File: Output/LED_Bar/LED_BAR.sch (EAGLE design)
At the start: 19 parts

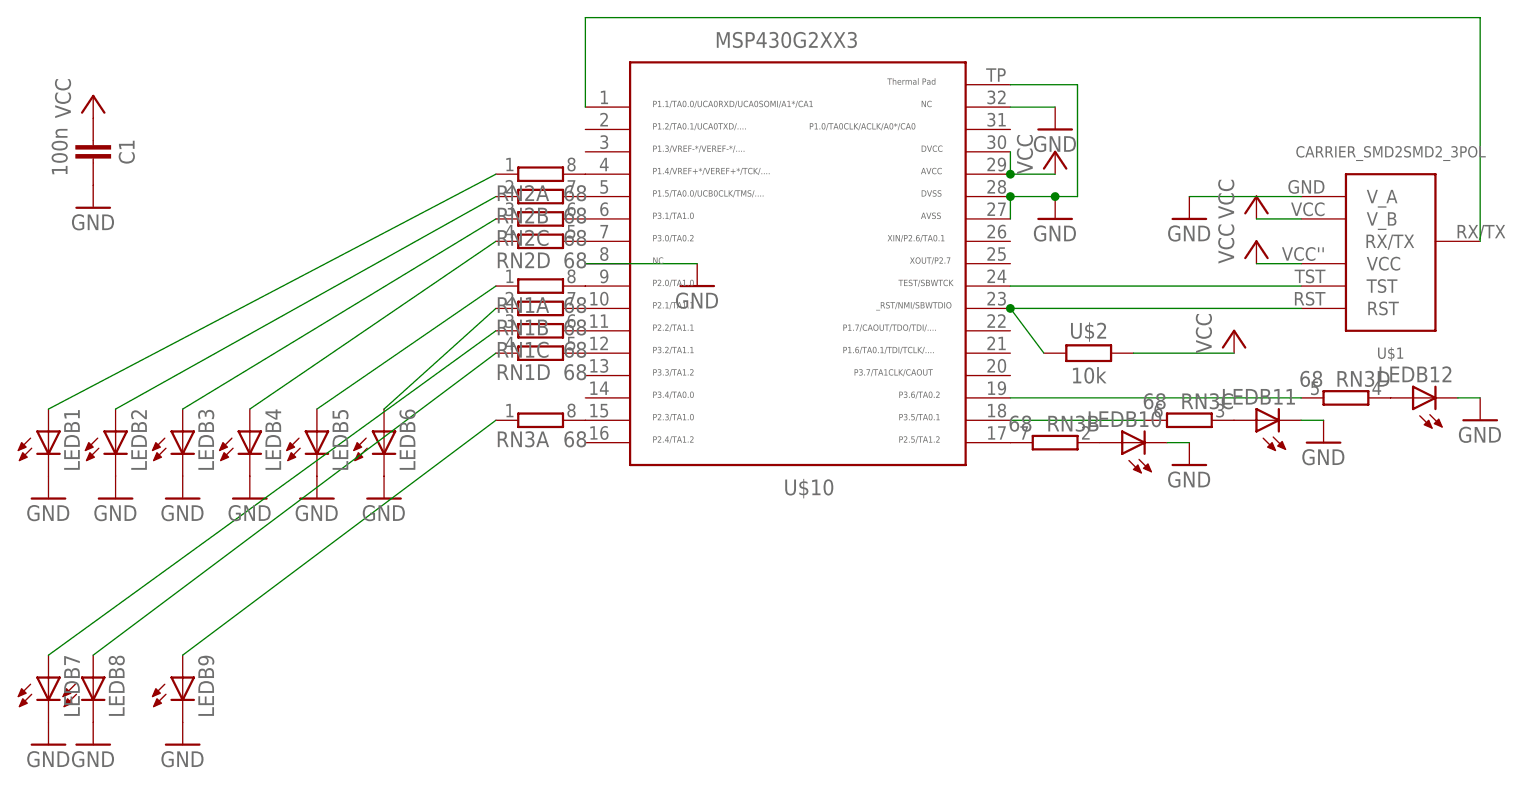
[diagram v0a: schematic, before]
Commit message: Update Pinheader
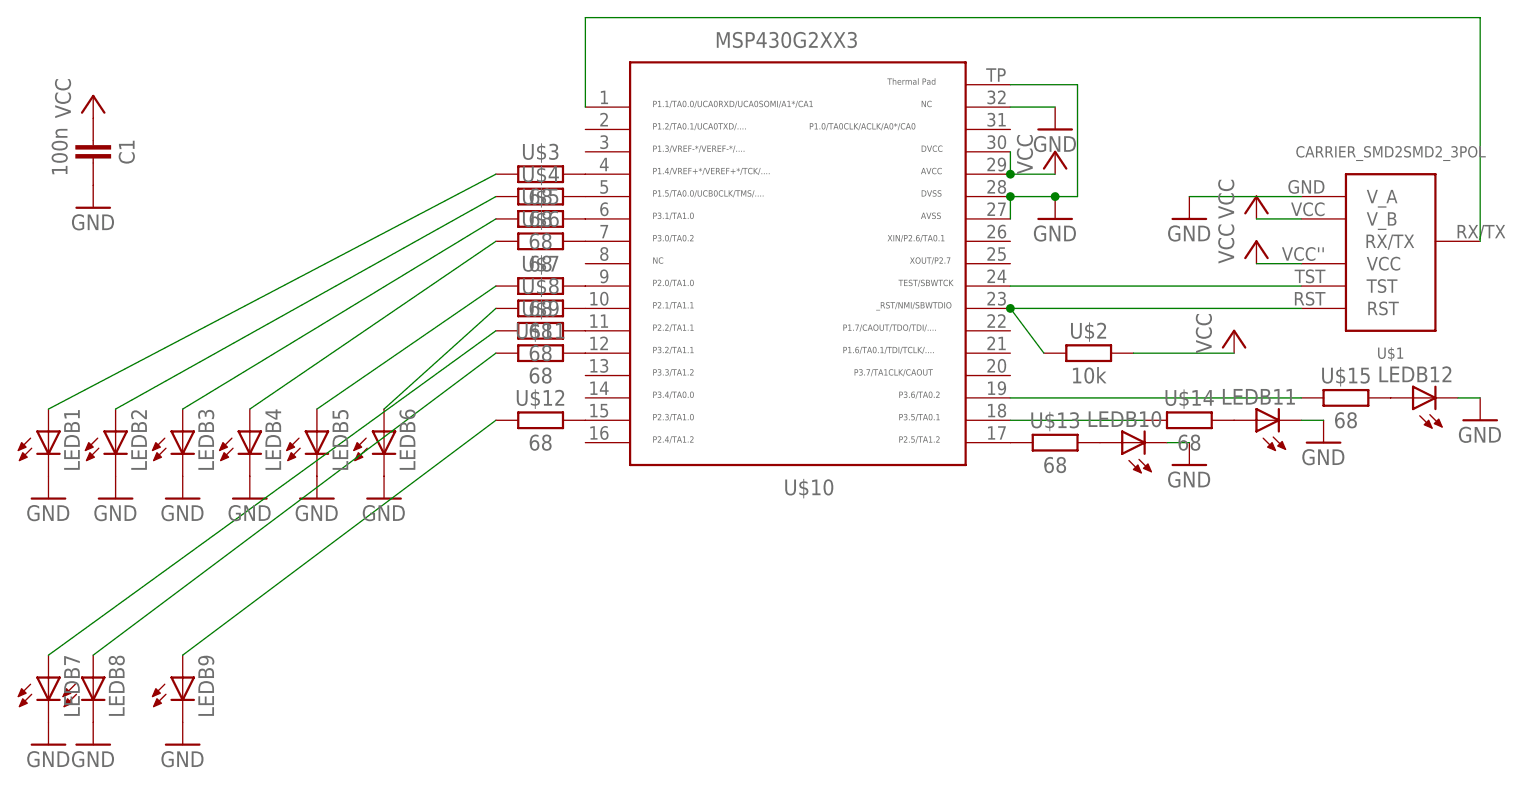
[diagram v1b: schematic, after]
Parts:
- removed RN1, RN2, RN3: 68, resistor-dil:4R-N0603-ARC
- added U$11, U$12, U$13, U$14, U$15, U$3, U$4, U$5, U$6, U$7, U$8, U$9: 68, thar:RESISTOR0603
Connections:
- net GND: no longer U$10.8
- net N$11: now also U$3.2; no longer RN2A.2
- net N$13: now also U$6.1; no longer RN2D.1
- net N$14: now also U$7.1; no longer RN1A.1
- net N$16: now also U$8.1; no longer RN1B.1
- net N$17: now also U$4.2; no longer RN2B.2
- net N$18: now also U$9.1; no longer RN1C.1
- net N$19: now also U$11.1; no longer RN1D.1
- net N$20: now also U$12.1; no longer RN3A.1
- net N$21: now also U$5.2; no longer RN2C.2
- net N$22: now also U$6.2; no longer RN2D.2
- net N$23: now also U$7.2; no longer RN1A.2
- net N$24: now also U$15.1; no longer RN3D.2
- net N$25: now also U$14.1; no longer RN3C.2
- net N$26: now also U$8.2; no longer RN1B.2
- net N$27: now also U$9.2; no longer RN1C.2
- net N$28: now also U$10.15, U$12.2; no longer RN1D.2, U$10.12
- net N$29: now also U$10.17, U$13.1; no longer RN3A.2, U$10.15
- net N$32: now also LEDB10.A, U$13.2; no longer RN3B.2, U$10.17
- net N$34: now also LEDB11.A, U$14.2; no longer LEDB10.A, RN3B.1
- net N$35: now also LEDB12.A, U$15.2; no longer LEDB11.A, RN3C.1
- net N$36: now also U$10.12, U$11.2; no longer LEDB12.A, RN3D.1
- net N$5: now also U$3.1; no longer RN2A.1
- net N$6: now also U$4.1; no longer RN2B.1
- net N$7: now also U$5.1; no longer RN2C.1
